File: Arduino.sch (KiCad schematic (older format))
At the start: 18 parts

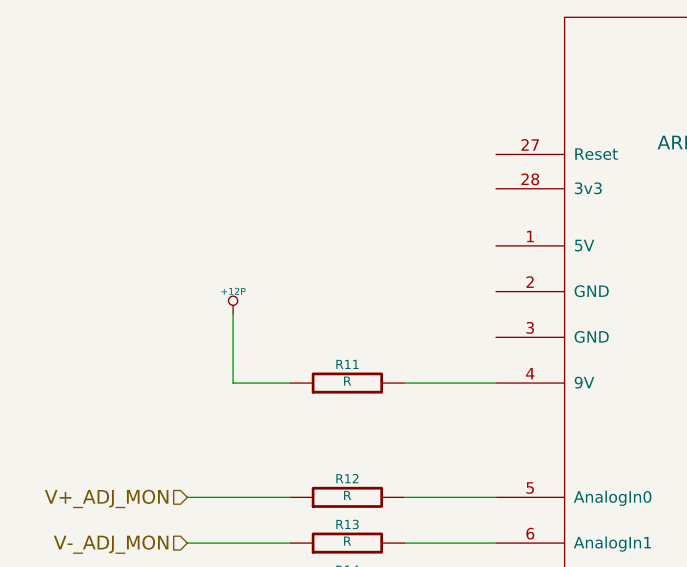
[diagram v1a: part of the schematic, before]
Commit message: 5.6 Associating and Placing the Arduino Module
Added Arduino and 0805_blob footprints, placed arduino board
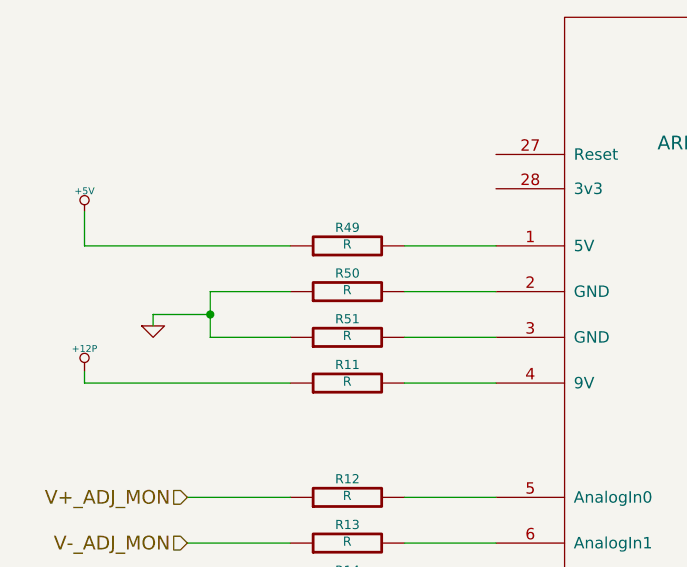
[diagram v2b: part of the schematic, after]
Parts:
- added R49, R50, R51: R, ~, symbol R
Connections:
- net GND: now also R50.1, R51.1
- net at uC1.1 (5V): now also R49.2
- net at uC1.2 (GND): now also R50.2
- net at uC1.3 (GND): now also R51.2
- new net +5V: R49.1
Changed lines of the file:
@@
 Relay-
 $Comp
-L GND #PWR29
+L GND #PWR028
 U 1 1 52F8F33B
 P 7900 5050
-F 0 "#PWR29" H 7900 5050 30  0001 C CNN
+F 0 "#PWR028" H 7900 5050 30  0001 C CNN
 F 1 "GND" H 7900 4980 30  0001 C CNN
 F 2 "" H 7900 5050 60  0000 C CNN
@@
 	2750 3500 2350 3500
 $Comp
-L +12P #PWR28
+L +12P #PWR029
 U 1 1 52F8980E
-P 1600 3200
-F 0 "#PWR28" H 1600 3170 30  0001 C CNN
-F 1 "+12P" H 1600 3300 30  0000 C CNN
-F 2 "" H 1600 3200 60  0000 C CNN
-F 3 "" H 1600 3200 60  0000 C CNN
-	1    1600 3200
-	1    0    0    -1
-$EndComp
-Wire Wire Line
-	1850 3500 1600 3500
-Wire Wire Line
-	1600 3500 1600 3200
+P 950 3450
+F 0 "#PWR029" H 950 3420 30  0001 C CNN
+F 1 "+12P" H 950 3550 30  0000 C CNN
+F 2 "" H 950 3450 60  0000 C CNN
+F 3 "" H 950 3450 60  0000 C CNN
+	1    950  3450
+	1    0    0    -1
+$EndComp
+Wire Wire Line
+	1850 3500 950  3500
+Wire Wire Line
+	950  3500 950  3450
 $Comp
 L ARDUINO uC1
@@
 Wire Wire Line
 	5400 4000 5150 4000
+$Comp
+L R R51
+U 1 1 530910A6
+P 2100 3300
+F 0 "R51" V 2180 3300 40  0000 C CNN
+F 1 "R" V 2107 3301 40  0000 C CNN
+F 2 "~" V 2030 3300 30  0000 C CNN
+F 3 "~" H 2100 3300 30  0000 C CNN
+	1    2100 3300
+	0    -1   -1   0
+$EndComp
+$Comp
+L R R50
+U 1 1 530910AC
+P 2100 3100
+F 0 "R50" V 2180 3100 40  0000 C CNN
+F 1 "R" V 2107 3101 40  0000 C CNN
+F 2 "~" V 2030 3100 30  0000 C CNN
+F 3 "~" H 2100 3100 30  0000 C CNN
+	1    2100 3100
+	0    -1   -1   0
+$EndComp
+$Comp
+L R R49
+U 1 1 530910B2
+P 2100 2900
+F 0 "R49" V 2180 2900 40  0000 C CNN
+F 1 "R" V 2107 2901 40  0000 C CNN
+F 2 "~" V 2030 2900 30  0000 C CNN
+F 3 "~" H 2100 2900 30  0000 C CNN
+	1    2100 2900
+	0    -1   -1   0
+$EndComp
+Wire Wire Line
+	2750 3100 2350 3100
+Wire Wire Line
+	2350 3300 2750 3300
+Wire Wire Line
+	1500 3300 1850 3300
+Wire Wire Line
+	1500 3100 1500 3300
+Wire Wire Line
+	1500 3100 1850 3100
+$Comp
+L GND #PWR030
+U 1 1 53091160
+P 1250 3250
+F 0 "#PWR030" H 1250 3250 30  0001 C CNN
+F 1 "GND" H 1250 3180 30  0001 C CNN
+F 2 "" H 1250 3250 60  0000 C CNN
+F 3 "" H 1250 3250 60  0000 C CNN
+	1    1250 3250
+	1    0    0    -1
+$EndComp
+Wire Wire Line
+	1500 3200 1250 3200
+Wire Wire Line
+	1250 3200 1250 3250
+Connection ~ 1500 3200
+Wire Wire Line
+	2750 2900 2350 2900
+$Comp
+L +5V #PWR031
+U 1 1 5309121F
+P 950 2750
+F 0 "#PWR031" H 950 2840 20  0001 C CNN
+F 1 "+5V" H 950 2840 30  0000 C CNN
+F 2 "" H 950 2750 60  0000 C CNN
+F 3 "" H 950 2750 60  0000 C CNN
+	1    950  2750
+	1    0    0    -1
+$EndComp
+Wire Wire Line
+	1850 2900 950  2900
+Wire Wire Line
+	950  2900 950  2750
 $EndSCHEMATC

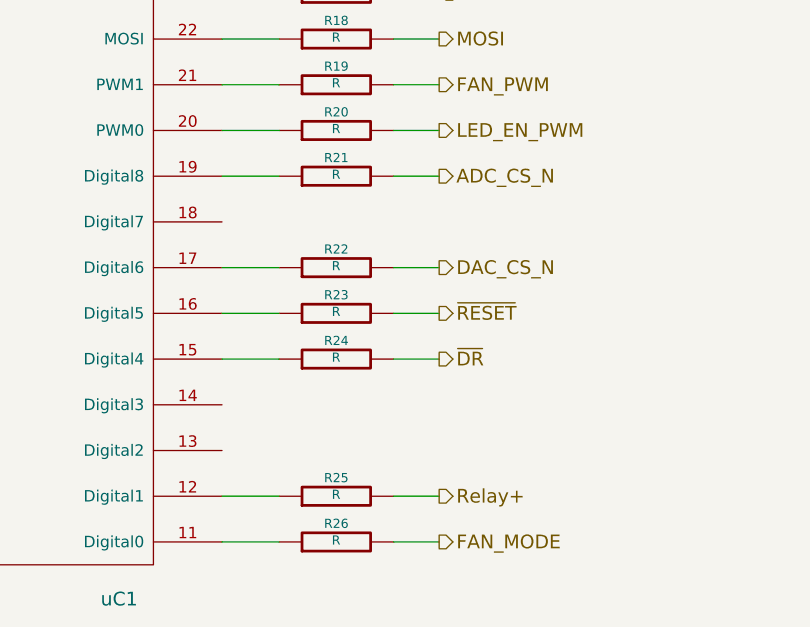
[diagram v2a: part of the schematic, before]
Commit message: 5.7 Video 1/2 Associating and Placing the Arduino Module
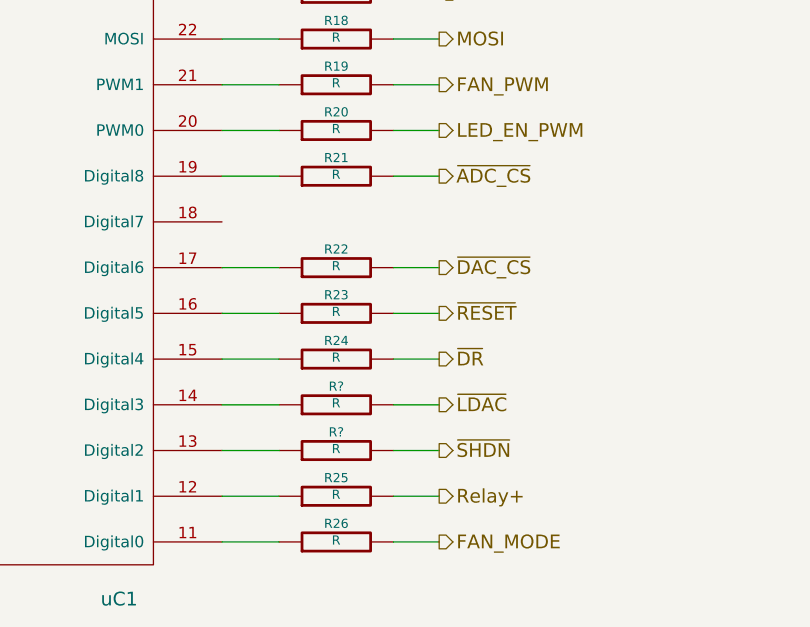
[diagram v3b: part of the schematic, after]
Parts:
- added R? (x2): R, ~, symbol R
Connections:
- net at uC1.13 (Digital2): now also R?.1
- net at uC1.14 (Digital3): now also R?.1
- net ADC_CS_N renamed ~ADC_CS
- net DAC_CS_N renamed ~DAC_CS
- new net ~LDAC: R?.2
- new net ~SHDN: R?.2
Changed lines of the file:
@@
 Sheet 7 9
 Title ""
-Date "22 feb 2014"
+Date "23 feb 2014"
 Rev ""
 Comp ""
@@
 SCLK
 Text HLabel 6100 3400 2    60   Output ~ 0
-ADC_CS_N
+~ADC_CS
 Text HLabel 6100 3000 2    60   Output ~ 0
 FAN_PWM
@@
 	5900 3000 6100 3000
 Text HLabel 6100 3800 2    60   Output ~ 0
-DAC_CS_N
+~DAC_CS
 $Comp
 L R R22
@@
 Wire Wire Line
 	950  2900 950  2750
+$Comp
+L R R?
+U 1 1 530A36E5
+P 5650 4600
+F 0 "R?" V 5730 4600 40  0000 C CNN
+F 1 "R" V 5657 4601 40  0000 C CNN
+F 2 "~" V 5580 4600 30  0000 C CNN
+F 3 "~" H 5650 4600 30  0000 C CNN
+	1    5650 4600
+	0    -1   -1   0
+$EndComp
+$Comp
+L R R?
+U 1 1 530A36EB
+P 5650 4400
+F 0 "R?" V 5730 4400 40  0000 C CNN
+F 1 "R" V 5657 4401 40  0000 C CNN
+F 2 "~" V 5580 4400 30  0000 C CNN
+F 3 "~" H 5650 4400 30  0000 C CNN
+	1    5650 4400
+	0    -1   -1   0
+$EndComp
+Wire Wire Line
+	5150 4400 5400 4400
+Wire Wire Line
+	5400 4600 5150 4600
+Text HLabel 6100 4400 2    60   Output ~ 0
+~LDAC
+Text HLabel 6100 4600 2    60   Output ~ 0
+~SHDN
+Wire Wire Line
+	5900 4400 6100 4400
+Wire Wire Line
+	6100 4600 5900 4600
 $EndSCHEMATC

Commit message: 5.7 Video 2/2 Associating and Placing the Arduino Module
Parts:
- gave numbers to parts that had none: 2
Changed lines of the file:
@@
 Relay-
 $Comp
-L GND #PWR028
+L GND #PWR35
 U 1 1 52F8F33B
 P 7900 5050
-F 0 "#PWR028" H 7900 5050 30  0001 C CNN
+F 0 "#PWR35" H 7900 5050 30  0001 C CNN
 F 1 "GND" H 7900 4980 30  0001 C CNN
 F 2 "" H 7900 5050 60  0000 C CNN
@@
 	2750 3500 2350 3500
 $Comp
-L +12P #PWR029
+L +12P #PWR33
 U 1 1 52F8980E
 P 950 3450
-F 0 "#PWR029" H 950 3420 30  0001 C CNN
+F 0 "#PWR33" H 950 3420 30  0001 C CNN
 F 1 "+12P" H 950 3550 30  0000 C CNN
 F 2 "" H 950 3450 60  0000 C CNN
@@
 	1500 3100 1850 3100
 $Comp
-L GND #PWR030
+L GND #PWR34
 U 1 1 53091160
 P 1250 3250
-F 0 "#PWR030" H 1250 3250 30  0001 C CNN
+F 0 "#PWR34" H 1250 3250 30  0001 C CNN
 F 1 "GND" H 1250 3180 30  0001 C CNN
 F 2 "" H 1250 3250 60  0000 C CNN
@@
 	2750 2900 2350 2900
 $Comp
-L +5V #PWR031
+L +5V #PWR32
 U 1 1 5309121F
 P 950 2750
-F 0 "#PWR031" H 950 2840 20  0001 C CNN
+F 0 "#PWR32" H 950 2840 20  0001 C CNN
 F 1 "+5V" H 950 2840 30  0000 C CNN
 F 2 "" H 950 2750 60  0000 C CNN
@@
 	950  2900 950  2750
 $Comp
-L R R?
+L R R53
 U 1 1 530A36E5
 P 5650 4600
-F 0 "R?" V 5730 4600 40  0000 C CNN
+F 0 "R53" V 5730 4600 40  0000 C CNN
 F 1 "R" V 5657 4601 40  0000 C CNN
 F 2 "~" V 5580 4600 30  0000 C CNN
@@
 $EndComp
 $Comp
-L R R?
+L R R52
 U 1 1 530A36EB
 P 5650 4400
-F 0 "R?" V 5730 4400 40  0000 C CNN
+F 0 "R52" V 5730 4400 40  0000 C CNN
 F 1 "R" V 5657 4401 40  0000 C CNN
 F 2 "~" V 5580 4400 30  0000 C CNN

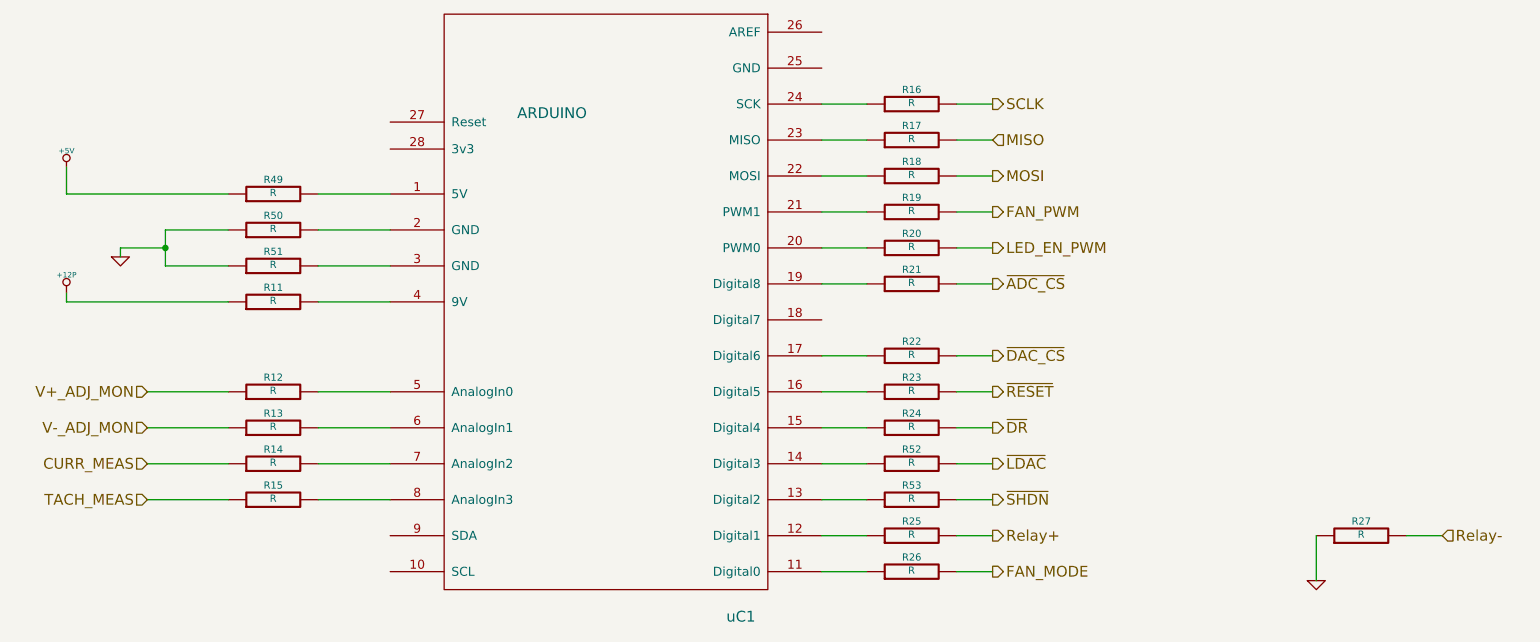
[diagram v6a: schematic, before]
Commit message: Cleanup/ERC checks, etc (on my own, no video)
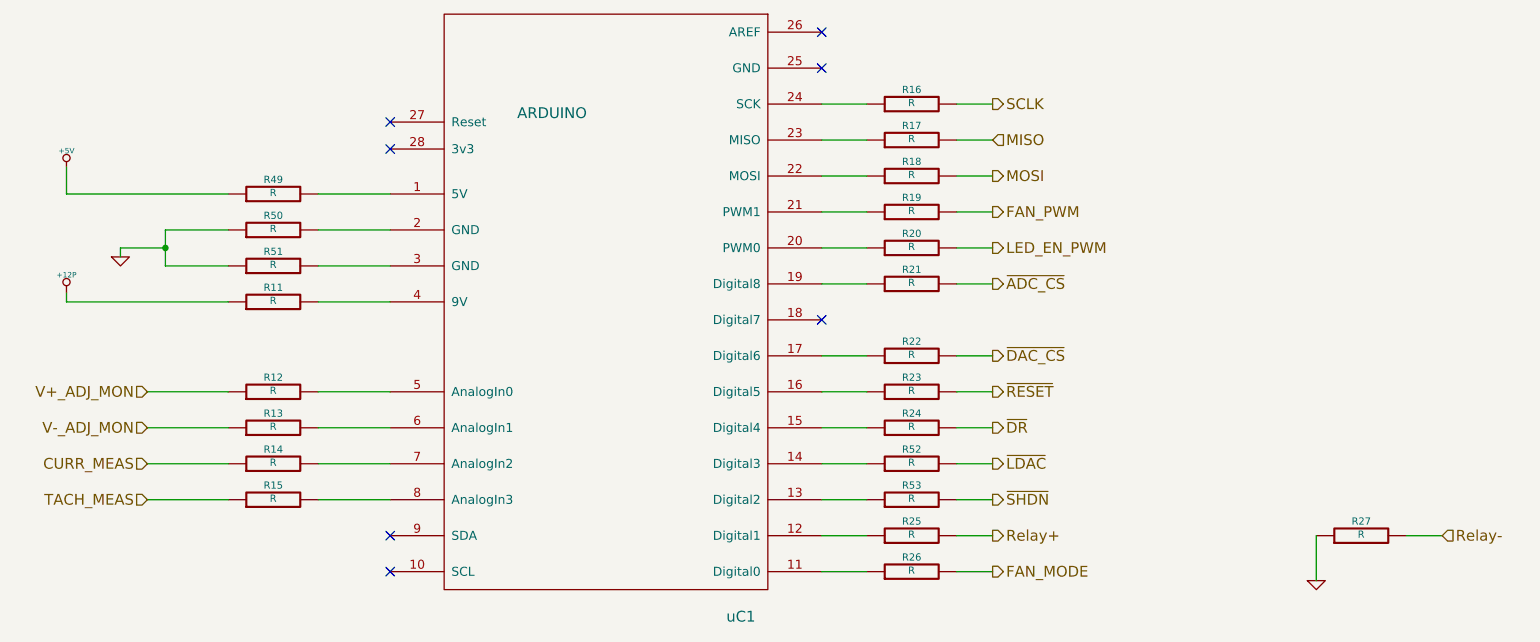
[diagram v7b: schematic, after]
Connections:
- no-connect marks 0 -> 7
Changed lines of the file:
@@
 Wire Wire Line
 	6100 4600 5900 4600
+NoConn ~ 2750 4800
+NoConn ~ 2750 5000
+NoConn ~ 2750 2500
+NoConn ~ 2750 2650
+NoConn ~ 5150 3600
+NoConn ~ 5150 2000
+NoConn ~ 5150 2200
 $EndSCHEMATC
